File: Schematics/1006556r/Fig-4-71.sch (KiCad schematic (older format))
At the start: 12 parts, among them J1 ConnectorGeneric, U1101 D3NOR-+3VDC-0VDC-nd1021041-1_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, U1102 D3NOR-+3VDC-0VDC-nd1021041-1_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, U1103 D3NOR-+3VDC-0VDC-nd1021041-1_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, U1104 D3NOR-+3VDC-0VDC-nd1021041-13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, U1105 D3NOR-NC-0VDC-expander-nd1021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, U1106 D3NOR-+3VDC-0VDC-nd1021041-13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, U1107 D3NOR-+3VDC-0VDC-nd1021041-13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, U1108 D3NOR-+3VDC-0VDC-nd1021041-13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, U1109 D3NOR-+3VDC-0VDC-nd1021041-13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, U1110 D3NOR-+3VDC-0VDC-nd1021041-13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, U1111 D3NOR-NC-0VDC-expander-nd1021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

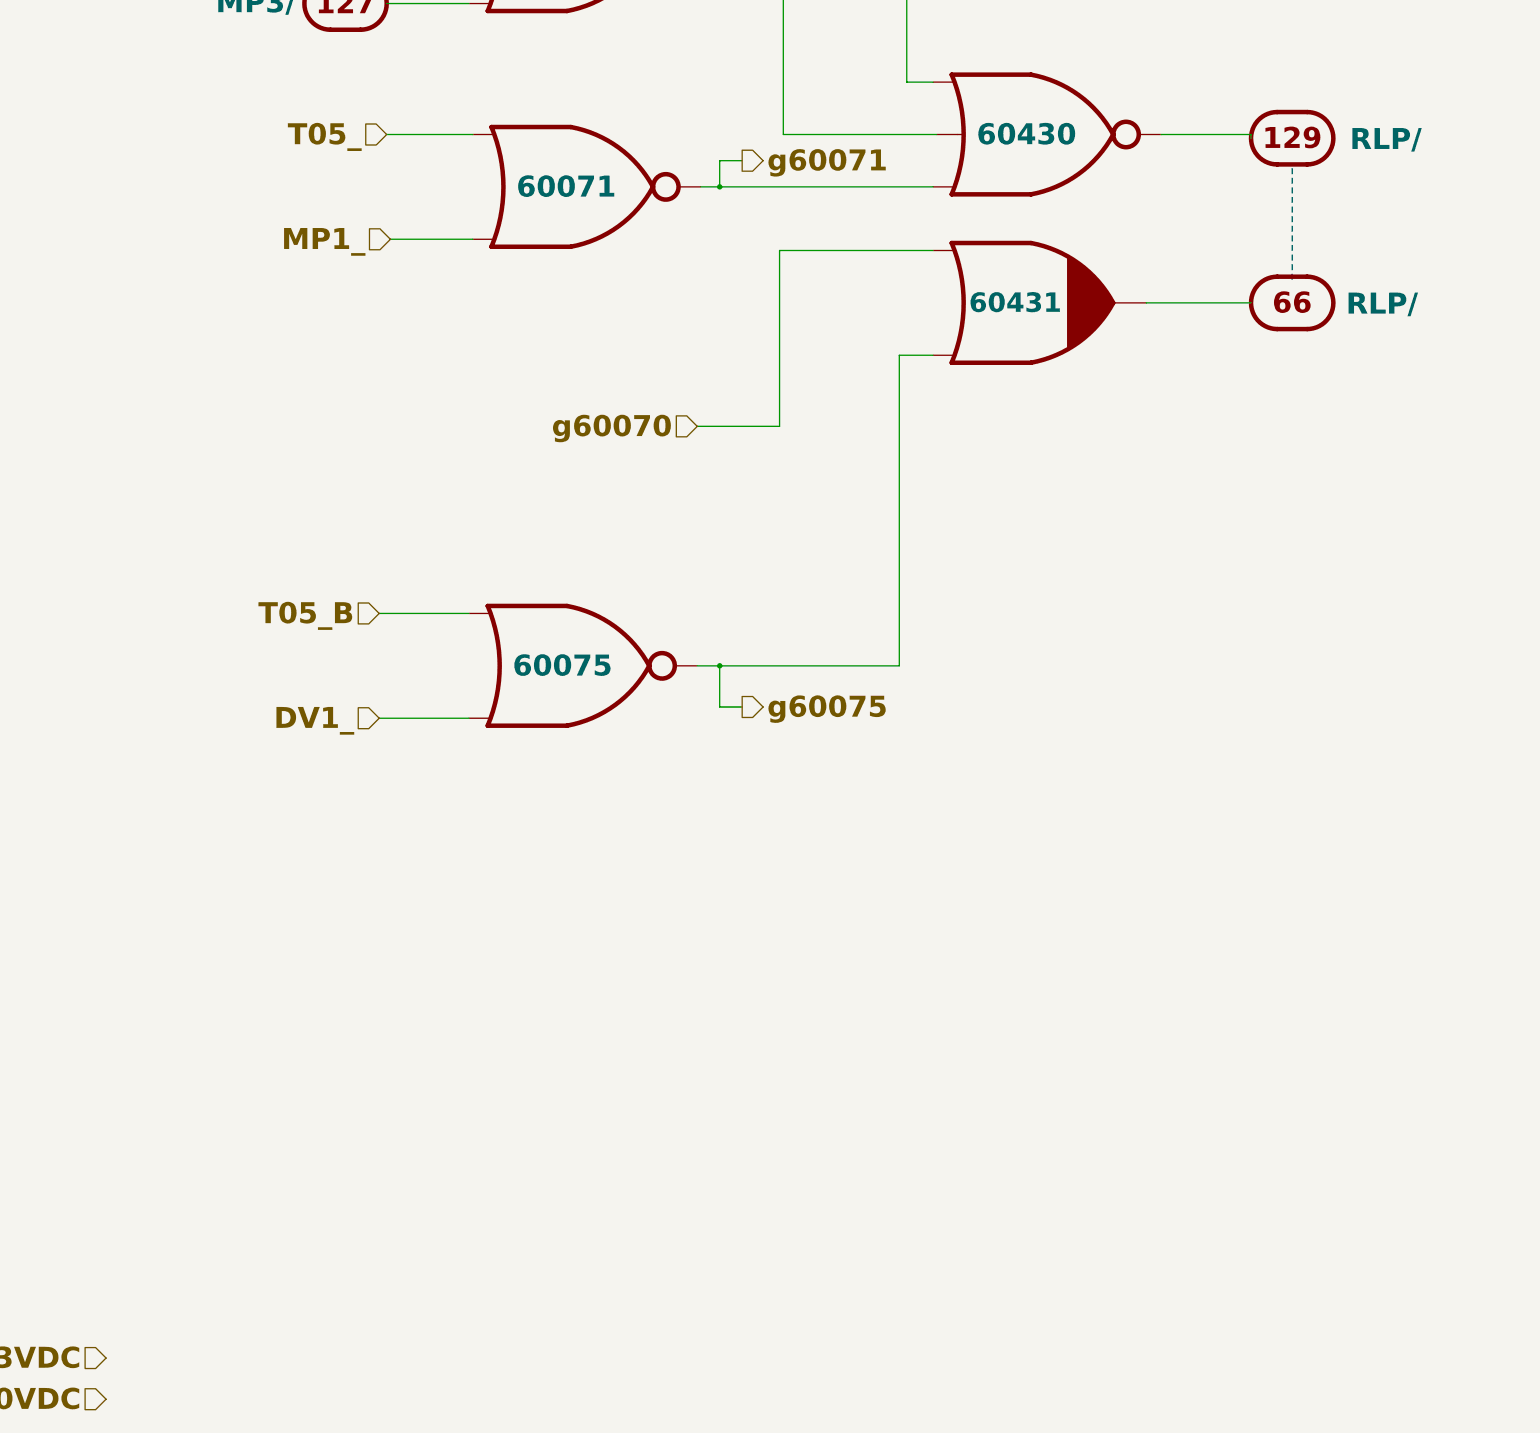
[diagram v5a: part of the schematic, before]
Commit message: Visual fixes were made using eelint, and some nominal electrical changes were made to accommodate current state of KiCad ERC capability. Nevertheless, ERC does not pass, due (I think) to current bugs in KiCad ERC.  Netlist changes are purely nominal, and relate to the addition of non-functional nodes in the power and ground nets.
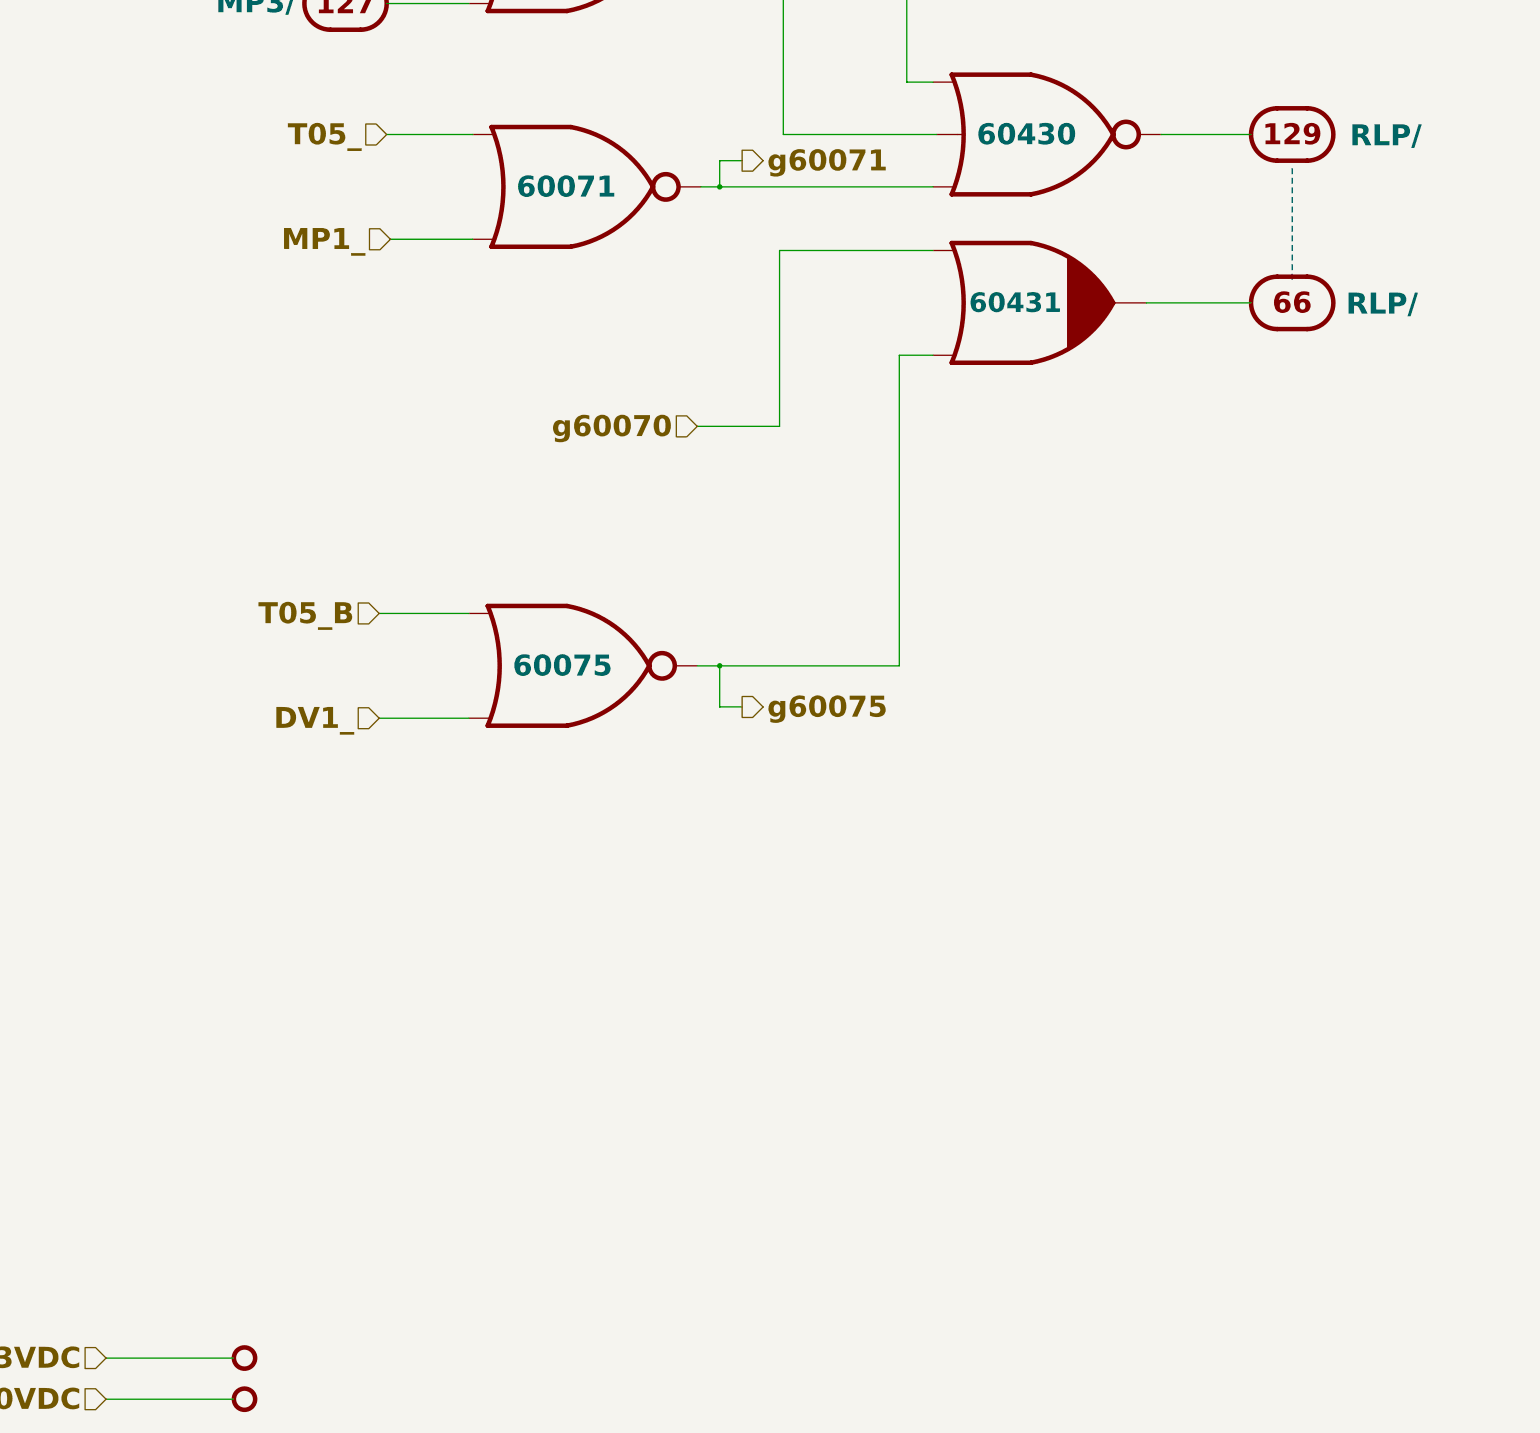
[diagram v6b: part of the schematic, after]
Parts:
- added N2401, N2402: Node2, symbol AGC_DSKY:Node2
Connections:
- net +3VDC: now also N2401.1
- net 0VDC: now also N2402.1
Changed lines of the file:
@@
-EESchema Schematic File Version 4
+EESchema Schematic File Version 5
 LIBS:module-cache
 EELAYER 29 0
@@
 L AGC_DSKY:ConnectorGeneric J1
 U 129 1 5BFA9696
-P 9525 7750
-F 0 "J1" H 9525 8075 140 0001 C CNN
-F 1 "ConnectorGeneric" H 9525 8175 140 0001 C CNN
-F 2 "" H 9525 8225 140 0001 C CNN
-F 3 "" H 9525 8225 140 0001 C CNN
-F 4 "RLP/" H 8900 7675 140 0000 C BNB "Caption"
-	129  9525 7750
+P 9525 7725
+F 0 "J1" H 9525 8050 140 0001 C CNN
+F 1 "ConnectorGeneric" H 9525 8150 140 0001 C CNN
+F 2 "" H 9525 8200 140 0001 C CNN
+F 3 "" H 9525 8200 140 0001 C CNN
+F 4 "RLP/" H 8900 7650 140 0000 C BNB "Caption"
+	129  9525 7725
 	-1   0    0    1
 $EndComp
@@
 Wire Wire Line
 	8650 7725 9250 7725
-Wire Wire Line
-	9250 7725 9250 7750
 Wire Wire Line
 	8550 8850 9250 8850
@@
 Text HLabel 3475 6150 0    140  Input ~ 28
 T02_
+$Comp
+L AGC_DSKY:Node2 N?
+U 1 1 5CE07FB3
+P 2525 15900
+AR Path="/5F3224B7/5CE07FB3" Ref="N?"  Part="1"
+AR Path="/5F3224CF/5CE07FB3" Ref="N2401"  Part="1"
+F 0 "N2401" H 2525 16000 50  0001 C CNN
+F 1 "Node2" H 2525 16075 50  0001 C CNN
+F 2 "" H 2525 15900 50  0001 C CNN
+F 3 "" H 2525 15900 50  0001 C CNN
+F 4 "+3VDC" H 2450 15900 140 0001 R CNB "Caption"
+	1    2525 15900
+	-1   0    0    1
+$EndComp
+$Comp
+L AGC_DSKY:Node2 N?
+U 1 1 5CE07FBC
+P 2525 16175
+AR Path="/5F3224B7/5CE07FBC" Ref="N?"  Part="0"
+AR Path="/5F3224CF/5CE07FBC" Ref="N2402"  Part="1"
+F 0 "N2402" H 2525 16275 50  0001 C CNN
+F 1 "Node2" H 2525 16350 50  0001 C CNN
+F 2 "" H 2525 16175 50  0001 C CNN
+F 3 "" H 2525 16175 50  0001 C CNN
+F 4 "0VDC" H 2450 16175 140 0001 R CNB "Caption"
+	1    2525 16175
+	-1   0    0    1
+$EndComp
+Wire Wire Line
+	1600 16175 2450 16175
+Wire Wire Line
+	1600 15900 2450 15900
 $EndSCHEMATC
